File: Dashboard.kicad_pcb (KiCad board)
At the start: 2 copper layers, 160 parts, among them J1 Left_Signal, J10 AccelConn, J11 BrakeConn, J12 AccelConn2, J13 BrakeConn2, J14 Motor-P, J15 Motor-C, J16 Array-C, J17 Array-P, J18 PowerConn, J19 CAN_OUT, J2 Right_Signal, J20 MotorCANConnector, J21 CAN_IN, J22 CAN_OUT, J23 USB_B_Micro, J24 ExtraGPIO_Conn, J25 UART_TP, J26 CAN_TP, J27 CAN_TP, J3 Brake Light, J4 Headlight, J5 MinionConn, J7 BPS_PWR, J8 JTAG, SW10 RESET, SW8 SW_Rotary2x6, SW9 KILL_SW, U1 EL3H7, U10 EL3H7, U11 EL3H7, U12 RI3-1205S, U13 NCP1117-3.3_SOT223, U14 ADM3055E, U15 CDSOT23-T24CAN, U16 LTC6820, U17 ADM3055E, U18 CDSOT23-T24CAN, U19 CP2102N-A01-GQFN24, U2 EL3H7, U20 HX1188FNL, U21 MCP23S17_SO, U3 EL3H7, U4 EL3H7, U5 EL3H7, U6 EL3H7, U7 STM32F413RHTx, U8 EL3H7, U9 EL3H7, Y1 Crystal

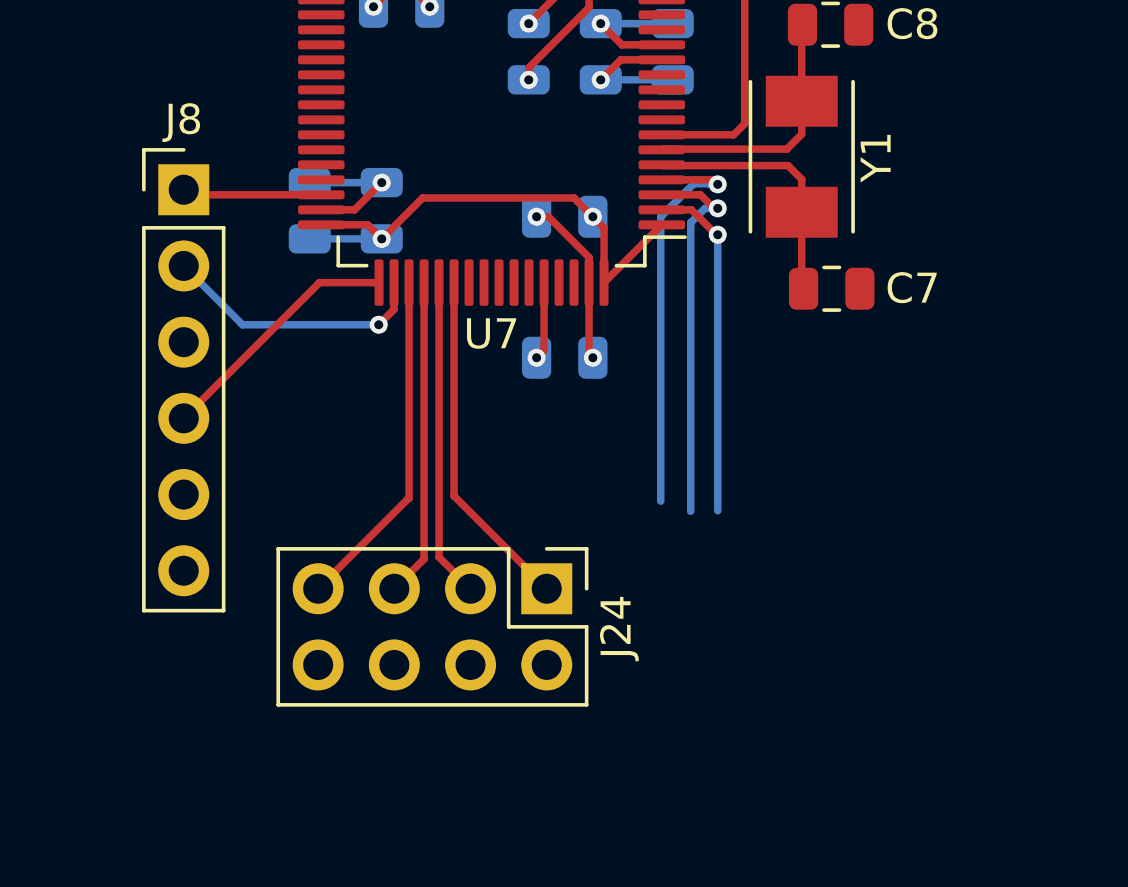
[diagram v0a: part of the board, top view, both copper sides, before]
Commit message: Adds components for the shift register and lays out modularized components
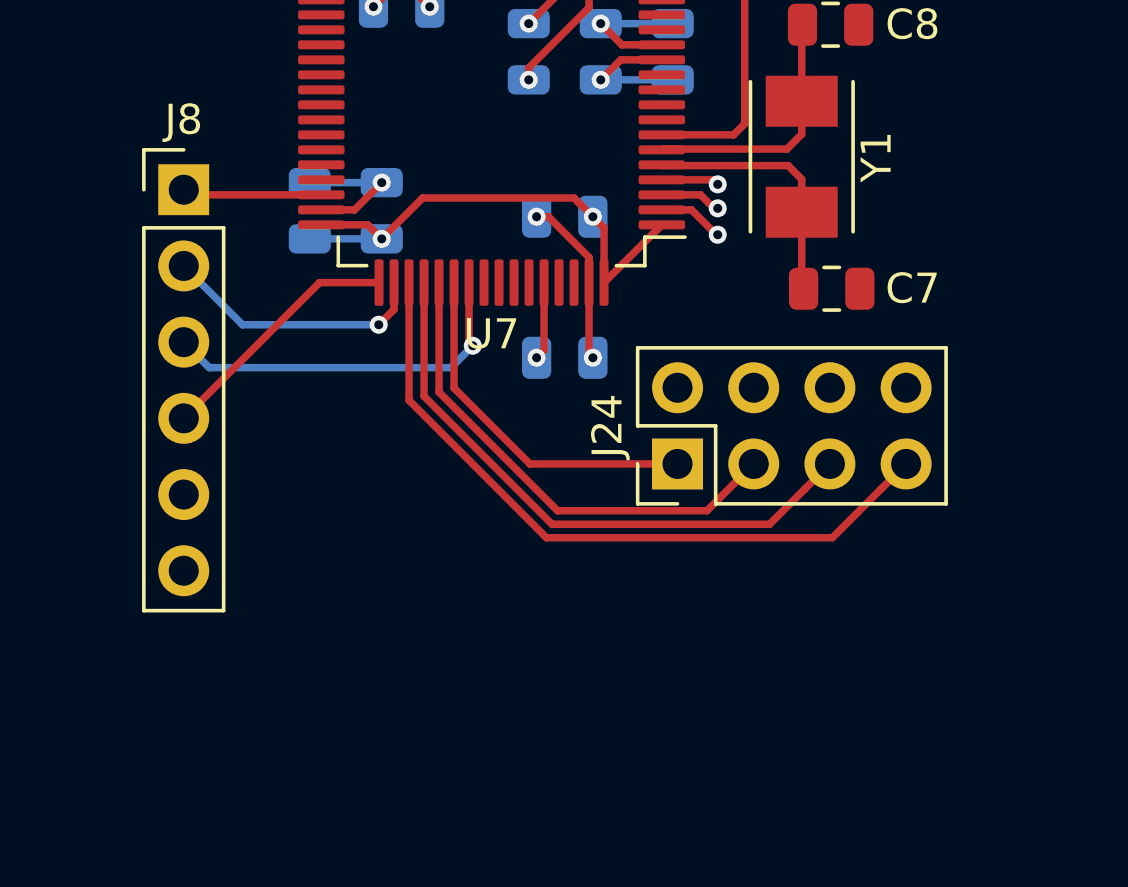
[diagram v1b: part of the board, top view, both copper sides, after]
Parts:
- moved J24 6.03 mm to (109.8, 119.6), turned to 90 degrees
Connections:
- J24 pad 4: /PC13 -> /PC15
- J24 pad 8: /PC15 -> /PC13
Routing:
- net /JTDO: track 0.00 -> 12.4 mm, vias 0 -> 1
- net /PC10: track 11.5 -> 23.4 mm
- net /PC15: track 13.8 -> 1.93 mm
- net /PC14: track 12.8 -> 2.05 mm
- net /PC11: track 10.6 -> 19.9 mm
- net /PC13: track 11.4 -> 2.21 mm
- net /PC12: track 10.6 -> 16.4 mm
- net /PD2: track 11.5 -> 12.0 mm
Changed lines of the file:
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@@
     (thickness 1.6)
     (drawings 0)
-    (tracks 750)
+    (tracks 755)
     (zones 0)
     (modules 160)
@@
   )
   (module Connector_PinHeader_2.54mm:PinHeader_2x04_P2.54mm_Vertical (layer F.Cu)
-    (at 105.4 123.8 270)
+    (at 109.76 119.64 90)
     (descr "Through hole straight pin header, 2x04, 2.54mm pitch, double rows")
     (tags "Through hole pin header THT 2x04 2.54mm double row")
@@
     (fp_line (start 3.81 -1.27) (end 3.81 8.89) (layer F.Fab) (width 0.1))
     (fp_line (start 0 -1.27) (end 3.81 -1.27) (layer F.Fab) (width 0.1))
-    (pad 8 thru_hole oval (at 2.54 7.62 270) (size 1.7 1.7) (drill 1) (layers *.Cu *.Mask)
-      (net 150 /PC15))
-    (pad 7 thru_hole oval (at 0 7.62 270) (size 1.7 1.7) (drill 1) (layers *.Cu *.Mask)
+    (pad 8 thru_hole oval (at 2.54 7.62 90) (size 1.7 1.7) (drill 1) (layers *.Cu *.Mask)
+      (net 152 /PC13))
+    (pad 7 thru_hole oval (at 0 7.62 90) (size 1.7 1.7) (drill 1) (layers *.Cu *.Mask)
       (net 149 /PC10))
-    (pad 6 thru_hole oval (at 2.54 5.08 270) (size 1.7 1.7) (drill 1) (layers *.Cu *.Mask)
+    (pad 6 thru_hole oval (at 2.54 5.08 90) (size 1.7 1.7) (drill 1) (layers *.Cu *.Mask)
       (net 151 /PC14))
-    (pad 5 thru_hole oval (at 0 5.08 270) (size 1.7 1.7) (drill 1) (layers *.Cu *.Mask)
+    (pad 5 thru_hole oval (at 0 5.08 90) (size 1.7 1.7) (drill 1) (layers *.Cu *.Mask)
       (net 148 /PC11))
-    (pad 4 thru_hole oval (at 2.54 2.54 270) (size 1.7 1.7) (drill 1) (layers *.Cu *.Mask)
-      (net 152 /PC13))
-    (pad 3 thru_hole oval (at 0 2.54 270) (size 1.7 1.7) (drill 1) (layers *.Cu *.Mask)
+    (pad 4 thru_hole oval (at 2.54 2.54 90) (size 1.7 1.7) (drill 1) (layers *.Cu *.Mask)
+      (net 150 /PC15))
+    (pad 3 thru_hole oval (at 0 2.54 90) (size 1.7 1.7) (drill 1) (layers *.Cu *.Mask)
       (net 147 /PC12))
-    (pad 2 thru_hole oval (at 2.54 0 270) (size 1.7 1.7) (drill 1) (layers *.Cu *.Mask)
+    (pad 2 thru_hole oval (at 2.54 0 90) (size 1.7 1.7) (drill 1) (layers *.Cu *.Mask)
       (net 177 "Net-(J24-Pad2)"))
-    (pad 1 thru_hole rect (at 0 0 270) (size 1.7 1.7) (drill 1) (layers *.Cu *.Mask)
+    (pad 1 thru_hole rect (at 0 0 90) (size 1.7 1.7) (drill 1) (layers *.Cu *.Mask)
       (net 146 /PD2))
     (model ${KISYS3DMOD}/Connector_PinHeader_2.54mm.3dshapes/PinHeader_2x04_P2.54mm_Vertical.wrl
@@
   (segment (start 97.825 113.595) (end 93.3 118.12) (width 0.25) (layer F.Cu) (net 36))
   (segment (start 99.81 113.595) (end 97.825 113.595) (width 0.25) (layer F.Cu) (net 36))
+  (via (at 102.935 115.7) (size 0.6) (drill 0.3) (layers F.Cu B.Cu) (net 37))
+  (segment (start 102.205001 116.429999) (end 102.935 115.7) (width 0.25) (layer B.Cu) (net 37))
+  (segment (start 93.3 115.58) (end 94.149999 116.429999) (width 0.25) (layer B.Cu) (net 37))
+  (segment (start 94.149999 116.429999) (end 102.205001 116.429999) (width 0.25) (layer B.Cu) (net 37))
+  (segment (start 102.81 115.575) (end 102.81 113.595) (width 0.25) (layer F.Cu) (net 37))
+  (segment (start 102.935 115.7) (end 102.81 115.575) (width 0.25) (layer F.Cu) (net 37))
   (via (at 99.8 115) (size 0.6) (drill 0.3) (layers F.Cu B.Cu) (net 38))
   (segment (start 100.31 113.595) (end 100.31 114.49) (width 0.25) (layer F.Cu) (net 38))
@@
   (segment (start 72.95 60.95) (end 73.45 60.95) (width 0.25) (layer F.Cu) (net 131))
   (segment (start 50.2 38.2) (end 72.95 60.95) (width 0.25) (layer F.Cu) (net 131))
-  (segment (start 102.31 120.71) (end 105.4 123.8) (width 0.25) (layer F.Cu) (net 146))
-  (segment (start 102.31 113.595) (end 102.31 120.71) (width 0.25) (layer F.Cu) (net 146))
-  (segment (start 101.81 122.75) (end 102.86 123.8) (width 0.25) (layer F.Cu) (net 147))
-  (segment (start 101.81 113.595) (end 101.81 122.75) (width 0.25) (layer F.Cu) (net 147))
-  (segment (start 101.31 122.81) (end 100.32 123.8) (width 0.25) (layer F.Cu) (net 148))
-  (segment (start 101.31 113.595) (end 101.31 122.81) (width 0.25) (layer F.Cu) (net 148))
-  (segment (start 100.81 113.595) (end 100.81 120.79) (width 0.25) (layer F.Cu) (net 149))
-  (segment (start 100.79 120.79) (end 97.78 123.8) (width 0.25) (layer F.Cu) (net 149))
-  (segment (start 100.81 120.79) (end 100.79 120.79) (width 0.25) (layer F.Cu) (net 149))
+  (segment (start 102.31 113.595) (end 102.31 117.11) (width 0.25) (layer F.Cu) (net 146))
+  (segment (start 104.84 119.64) (end 109.76 119.64) (width 0.25) (layer F.Cu) (net 146))
+  (segment (start 102.31 117.11) (end 104.84 119.64) (width 0.25) (layer F.Cu) (net 146))
+  (segment (start 101.81 117.24641) (end 105.76359 121.2) (width 0.25) (layer F.Cu) (net 147))
+  (segment (start 101.81 113.595) (end 101.81 117.24641) (width 0.25) (layer F.Cu) (net 147))
+  (segment (start 110.74 121.2) (end 112.3 119.64) (width 0.25) (layer F.Cu) (net 147))
+  (segment (start 105.76359 121.2) (end 110.74 121.2) (width 0.25) (layer F.Cu) (net 147))
+  (segment (start 113.990001 120.489999) (end 114.84 119.64) (width 0.25) (layer F.Cu) (net 148))
+  (segment (start 112.82999 121.65001) (end 113.990001 120.489999) (width 0.25) (layer F.Cu) (net 148))
+  (segment (start 105.57719 121.65001) (end 112.82999 121.65001) (width 0.25) (layer F.Cu) (net 148))
+  (segment (start 101.31 117.38282) (end 105.57719 121.65001) (width 0.25) (layer F.Cu) (net 148))
+  (segment (start 101.31 113.595) (end 101.31 117.38282) (width 0.25) (layer F.Cu) (net 148))
+  (segment (start 100.81 113.595) (end 100.81 117.51923) (width 0.25) (layer F.Cu) (net 149))
+  (segment (start 116.530001 120.489999) (end 117.38 119.64) (width 0.25) (layer F.Cu) (net 149))
+  (segment (start 114.91998 122.10002) (end 116.530001 120.489999) (width 0.25) (layer F.Cu) (net 149))
+  (segment (start 105.39079 122.10002) (end 114.91998 122.10002) (width 0.25) (layer F.Cu) (net 149))
+  (segment (start 100.81 117.51923) (end 105.39079 122.10002) (width 0.25) (layer F.Cu) (net 149))
   (segment (start 110.95001 110.17) (end 111.1 110.31999) (width 0.25) (layer F.Cu) (net 150))
   (segment (start 109.235 110.17) (end 110.95001 110.17) (width 0.25) (layer F.Cu) (net 150))
   (via (at 111.1 110.31999) (size 0.6) (drill 0.3) (layers F.Cu B.Cu) (net 150))
-  (segment (start 110.839329 110.31999) (end 110.819339 110.3) (width 0.25) (layer B.Cu) (net 150))
-  (segment (start 111.1 110.31999) (end 110.839329 110.31999) (width 0.25) (layer B.Cu) (net 150))
-  (segment (start 110.819339 110.3) (end 110.3 110.3) (width 0.25) (layer B.Cu) (net 150))
-  (segment (start 109.2 111.4) (end 109.2 120.88) (width 0.25) (layer B.Cu) (net 150))
-  (segment (start 110.3 110.3) (end 109.2 111.4) (width 0.25) (layer B.Cu) (net 150))
   (segment (start 110.975001 111.119993) (end 111.1 111.119993) (width 0.25) (layer F.Cu) (net 151))
   (via (at 111.1 111.119993) (size 0.6) (drill 0.3) (layers F.Cu B.Cu) (net 151))
   (segment (start 109.235 110.67) (end 110.525008 110.67) (width 0.25) (layer F.Cu) (net 151))
   (segment (start 110.525008 110.67) (end 110.975001 111.119993) (width 0.25) (layer F.Cu) (net 151))
-  (segment (start 110.675736 111.119993) (end 111.1 111.119993) (width 0.25) (layer B.Cu) (net 151))
-  (segment (start 110.2 111.595729) (end 110.675736 111.119993) (width 0.25) (layer B.Cu) (net 151))
-  (segment (start 110.2 121.217919) (end 110.2 111.595729) (width 0.25) (layer B.Cu) (net 151))
   (via (at 111.1 112) (size 0.6) (drill 0.3) (layers F.Cu B.Cu) (net 152))
   (segment (start 111.055005 112) (end 111.1 112) (width 0.25) (layer F.Cu) (net 152))
-  (segment (start 109.235 111.17) (end 110.225005 111.17) (width 0.25) (layer F.Cu) (net 152))
   (segment (start 110.225005 111.17) (end 111.055005 112) (width 0.25) (layer F.Cu) (net 152))
-  (segment (start 111.1 112) (end 111.1 121.2) (width 0.25) (layer B.Cu) (net 152))
+  (segment (start 109.235 111.17) (end 110.225005 111.17) (width 0.25) (layer F.Cu) (net 152))
   (segment (start 59.5375 123.3625) (end 59.95 122.95) (width 0.3048) (layer F.Cu) (net 154))
   (segment (start 59.5375 125.6) (end 59.5375 123.3625) (width 0.3048) (layer F.Cu) (net 154))

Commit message: Lays out PCB for Controls leader board
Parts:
- removed U21: MCP23S17_SO, Package_SO:SOIC-28W_7.5x17.9mm_P1.27mm
- LOGO1: footprint UTSVT_Special:Hallock_Image_Small -> UTSVT_Special:Hallock_Image; moved to B.Cu
- moved H2 232.1 mm to (204.5, 56.5)
- moved H3 231.3 mm to (204.5, 172.0)
- moved J18 210.2 mm to (36.0, 105.5), turned to 90 degrees
- moved TP6 208.9 mm to (35.4, 112.9), turned to 180 degrees
- moved TP3 199.8 mm to (42.5, 100.6), turned to 180 degrees
- moved TP2 196.9 mm to (42.5, 106.9), turned to 180 degrees
- moved U13 196.0 mm to (41.9, 112.9), turned to 180 degrees
- moved C22 194.7 mm to (41.8, 119.5), turned to 0 degrees
- moved C20 188.7 mm to (47.4, 103.8), turned to 90 degrees
- moved SW9 185.2 mm to (202.5, 134.3), turned to 270 degrees
- moved D1 182.2 mm to (202.5, 120.6), turned to 270 degrees
- moved C21 181.8 mm to (49.6, 110.0), turned to 90 degrees
- moved R29 180.4 mm to (49.6, 114.3), turned to 270 degrees
- moved D14 179.4 mm to (49.6, 118.6), turned to 90 degrees
- moved R12 175.9 mm to (197.7, 129.0), turned to 90 degrees
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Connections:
- J24 pad 1: /PD2 -> /PB7
- J24 pad 3: /PC12 -> /PB6
- J24 pad 5: /PC11 -> /PB5
- J24 pad 7: /PC10 -> /PB4
- J25 pad 1: /UART3_Tx -> /UART2_Tx
- J25 pad 2: /UART3_Rx -> /UART2_Rx
- J5 pad 3: /UART2_Rx -> /UART3_Tx
- J5 pad 4: /UART2_Tx -> /UART3_Rx
- U16 pad 4: /SCK -> /CLK
- U19 pad 20: /UART3_Rx -> /UART2_Rx
- U19 pad 21: /UART3_Tx -> /UART2_Tx
- U7 pad 10: /M_PRCHG -> /M_CNCTR
- U7 pad 11: /M_CNCTR -> /M_PRCHG
- U7 pad 14: Net-(U7-Pad14) -> /IG2
- U7 pad 15: Net-(U7-Pad15) -> /IG1
- U7 pad 20: /CTRL_FAULT -> /CS
- U7 pad 21: /LEFT_BLINK -> /CLK
- U7 pad 22: /RIGHT_BLINK -> /MISO
- U7 pad 23: /Headlight_ON -> /MOSI
- U7 pad 24: /BPS_FAULT -> Net-(U7-Pad24)
- U7 pad 26: /BK_LIGHT -> Net-(U7-Pad26)
- U7 pad 27: /IG1 -> Net-(U7-Pad27)
- U7 pad 28: /IG2 -> Net-(U7-Pad28)
- U7 pad 35: /CRUZ_ST -> Net-(U7-Pad35)
- U7 pad 36: /CRUZ_EN -> Net-(U7-Pad36)
- U7 pad 37: /HZD_SW -> /Headlight_ON
- U7 pad 38: /FR_SW -> /BK_LIGHT
- U7 pad 39: /Headlight_SW -> /RIGHT_BLINK
- U7 pad 40: /LEFT_SW -> /LEFT_BLINK
- U7 pad 41: /RIGHT_SW -> Net-(U7-Pad41)
- U7 pad 42: /RSVD_LED -> Net-(U7-Pad42)
- U7 pad 51: /PC10 -> /Accel_Pot
- U7 pad 52: /PC11 -> /Brake_Pot
- U7 pad 53: /PC12 -> /Accel_Pot2
- U7 pad 54: /PD2 -> /Brake_Pot2
- U7 pad 56: /Accel_Pot -> /PB4
- U7 pad 57: /Brake_Pot -> /PB5
- U7 pad 58: /Accel_Pot2 -> /PB6
- U7 pad 59: /Brake_Pot2 -> /PB7
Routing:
- net +3V3: track 141.0 -> 533.0 mm, vias 14 -> 22
- net GNDPWR: track 50.9 -> 294.5 mm, vias 6 -> 8
- net /M_PRCHG: track 0.00 -> 152.4 mm, vias 0 -> 2
- net /M_CNCTR: track 0.00 -> 141.1 mm, vias 0 -> 2
- net /A_CNCTR: track 0.00 -> 129.8 mm, vias 0 -> 2
- net /A_PRCHG: track 0.00 -> 123.7 mm, vias 0 -> 2
- net /Brake_Pot2: track 10.1 -> 126.6 mm
- net /UART2_Tx: track 0.00 -> 114.3 mm, vias 0 -> 1
- net /UART2_Rx: track 0.00 -> 113.4 mm, vias 0 -> 1
- net /Accel_Pot2: track 10.1 -> 110.1 mm
- net /Brake_Pot: track 10.1 -> 93.2 mm
- net +12V: track 38.8 -> 120.1 mm, vias 4 -> 5
- net +5V: track 42.5 -> 117.5 mm, vias 1 -> 3
- net /CAN_Rx: track 0.00 -> 69.7 mm
- net /CAN_Tx: track 0.00 -> 67.0 mm
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- added copper zone on B.Cu, net +12V
- added copper zone on B.Cu, net +5V
- added copper zone on B.Cu, net GND
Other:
- board outline added: 176.5 x 121.5 mm
- board text added: "Dr. Gary Hallock"
- board text added: "UTSVT - Controls Leader Board v2.0 Fall 2020"

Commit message: Adds SPI header to test
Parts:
- added J6: SPI, Connector_PinHeader_2.54mm:PinHeader_1x04_P2.54mm_Vertical, F.Cu at (123.1, 79.0)
- moved LOGO2 3.31 mm to (158.7, 81.1)
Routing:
- net GND: track 121.3 -> 163.4 mm, vias 19 -> 20
- net /CS: track 33.8 -> 54.0 mm
- net /CLK: track 33.8 -> 52.1 mm
- net /MISO: track 33.8 -> 50.1 mm
- net /MOSI: track 33.8 -> 48.8 mm
- net GNDPWR: track 294.5 -> 303.2 mm
- net +5V: track 117.5 -> 122.0 mm, vias 3 -> 5
- added copper zone on B.Cu, net (none)
- removed copper zone on B.Cu, net GND
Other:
- board text added: "Exterior Lights"

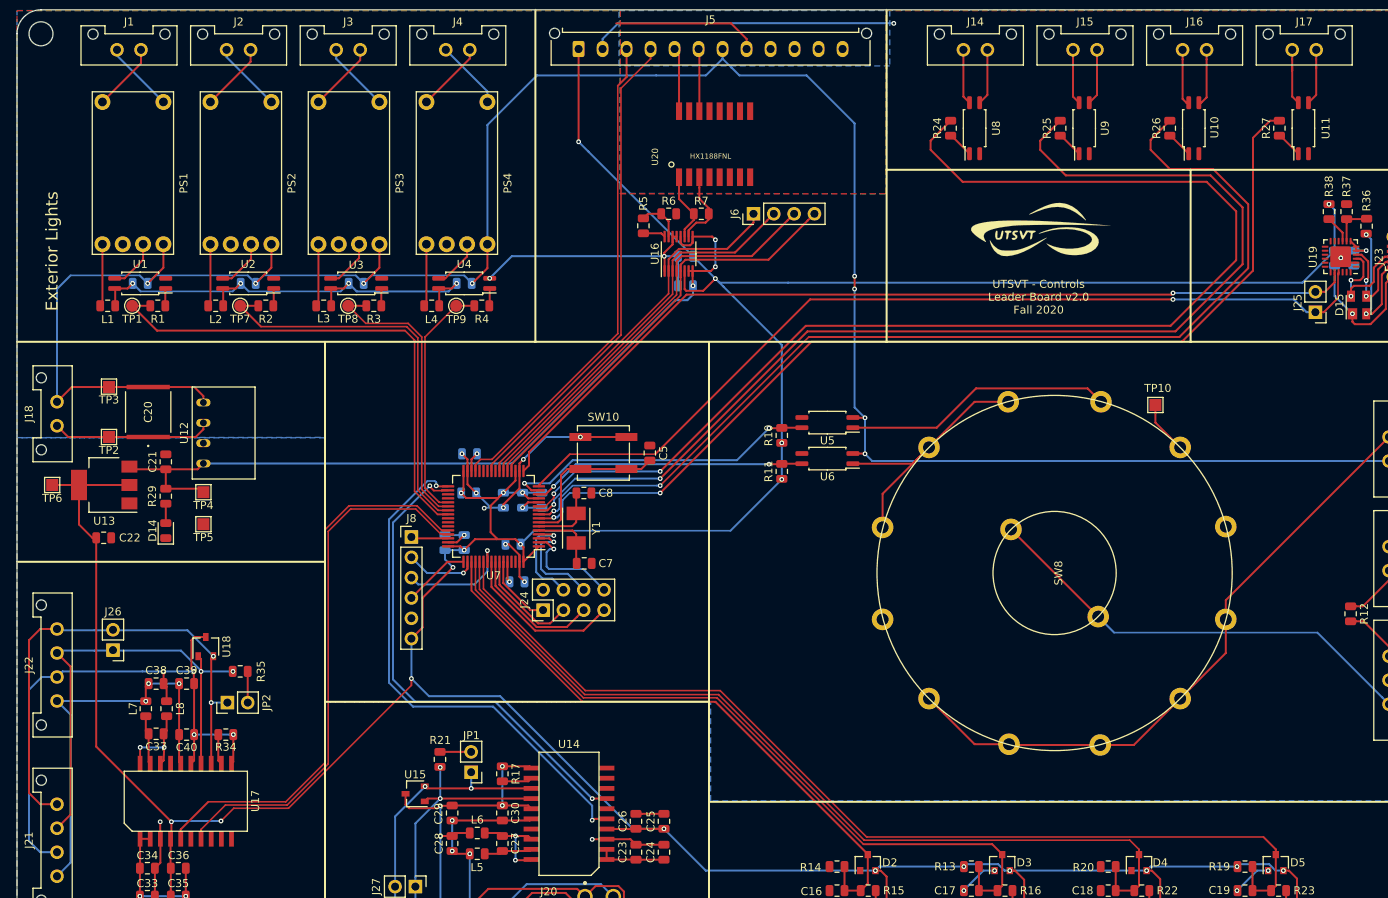
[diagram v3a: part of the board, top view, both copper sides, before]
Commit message: Makes all traces .25 mm
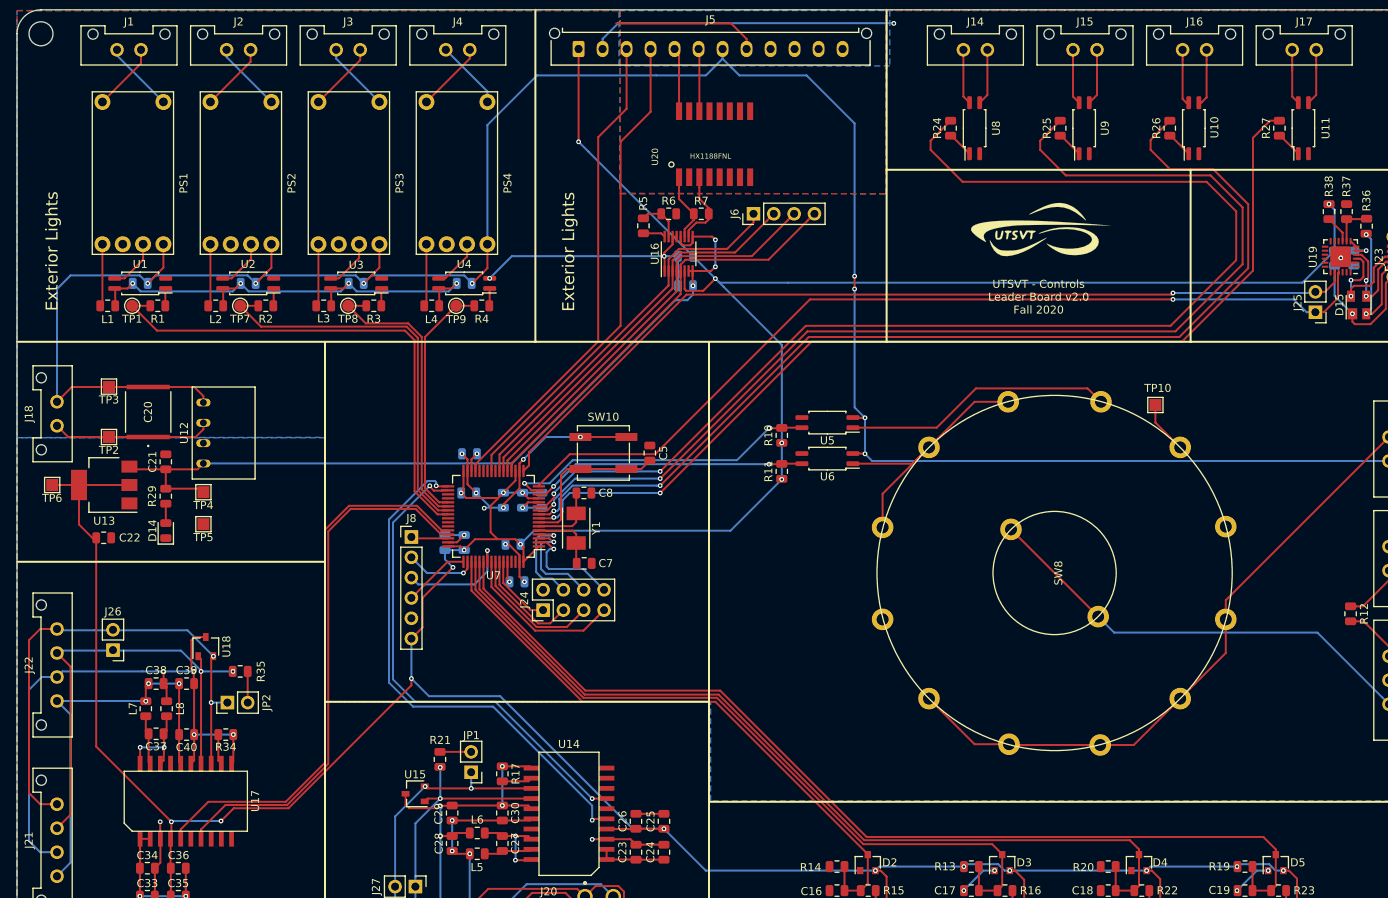
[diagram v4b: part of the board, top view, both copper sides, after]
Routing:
- net /UART3_Tx: track 61.4 -> 60.6 mm
- net /CS: track 54.0 -> 54.8 mm
